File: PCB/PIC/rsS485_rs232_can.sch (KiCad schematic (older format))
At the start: 50 parts, among them J2 TB_1X3, J3 DB9, J4 TB_1X3, U5 MAX3072, U6 ST3232E, U7 MCP2551, U8 PESD1CAN

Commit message: Correcciones al esquematico segun rev01
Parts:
- removed R42, R45: 1K5, ~, symbol R_MINI
- removed U7: MCP2551, ~, symbol MCP2551
- added U7: VP231, footprints:-SOIC8, symbol VP231
- C21, C28: value 10uF / 6V3 -> 10uF/6V3
- D8: footprint ~ -> (none)
- J2, J4: footprint (none) -> footprints:bornier3
- J3: footprint (none) -> footprints:K22X-E9P-NJ
- JP1, JP2, JP3, JP4, JP5, JP6: symbol JUMPER-2 -> Jumper-2
- PS1, PS2: symbol R -> R-RESCUE-ciaa-pic
- U8: footprint (none) -> footprints:SOT23
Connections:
- wire segments 147 -> 144
- no-connect marks 3 -> 5
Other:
- note added: "Quien hizo el 485 y el CAN quería forzar\nla vista del lector. Tamaños de textos estan achicados."
- note added: "SN65HVD230 - 231"
- moved on the sheet: C21, C22, C23, C24, C25, C26, C27, C28, C29, C30, D6, D7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

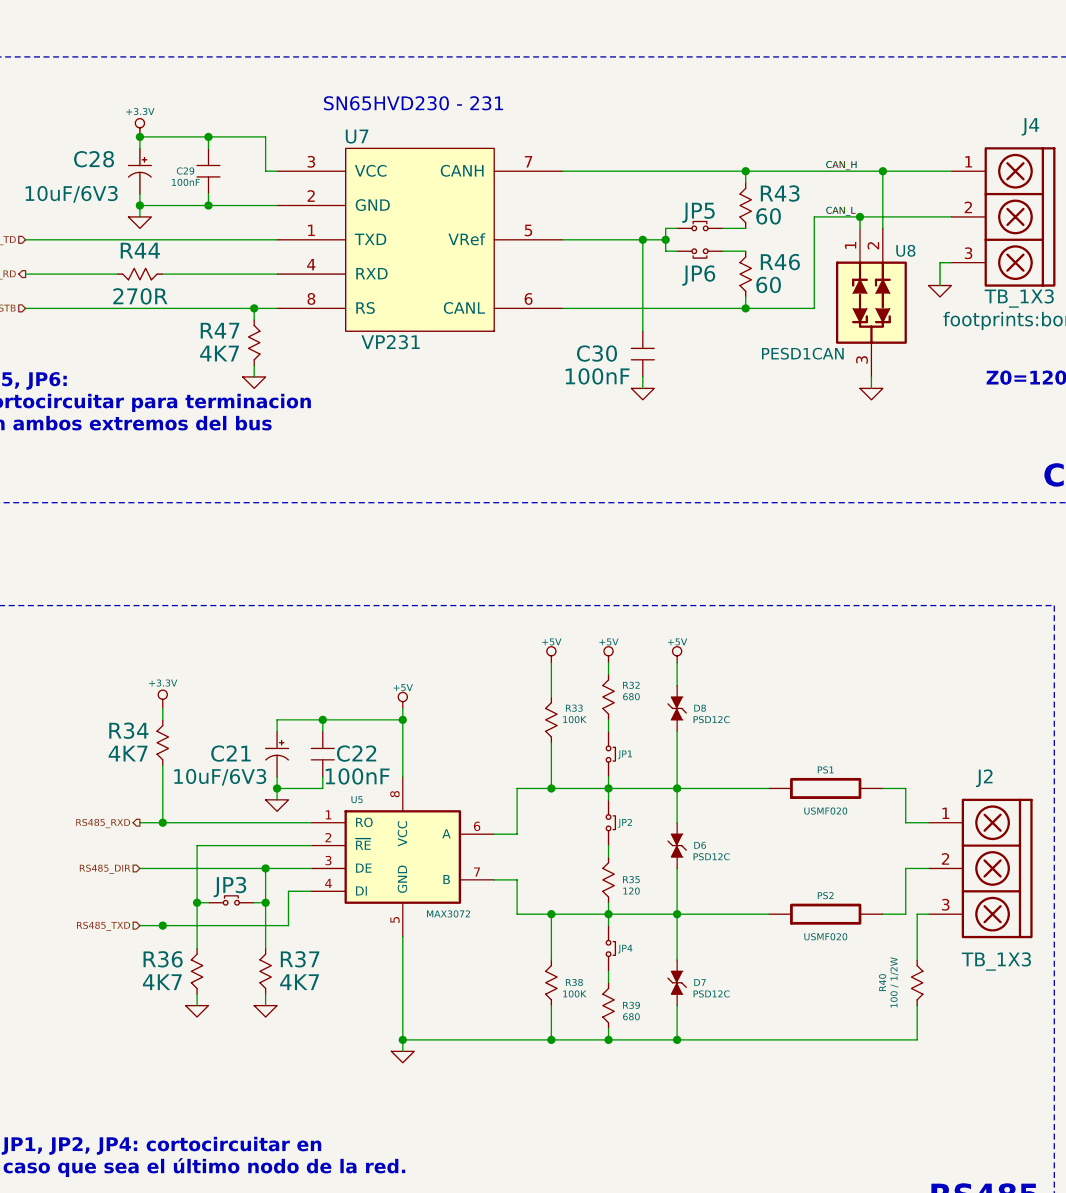
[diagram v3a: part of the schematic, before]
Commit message: elimino conector salida reles
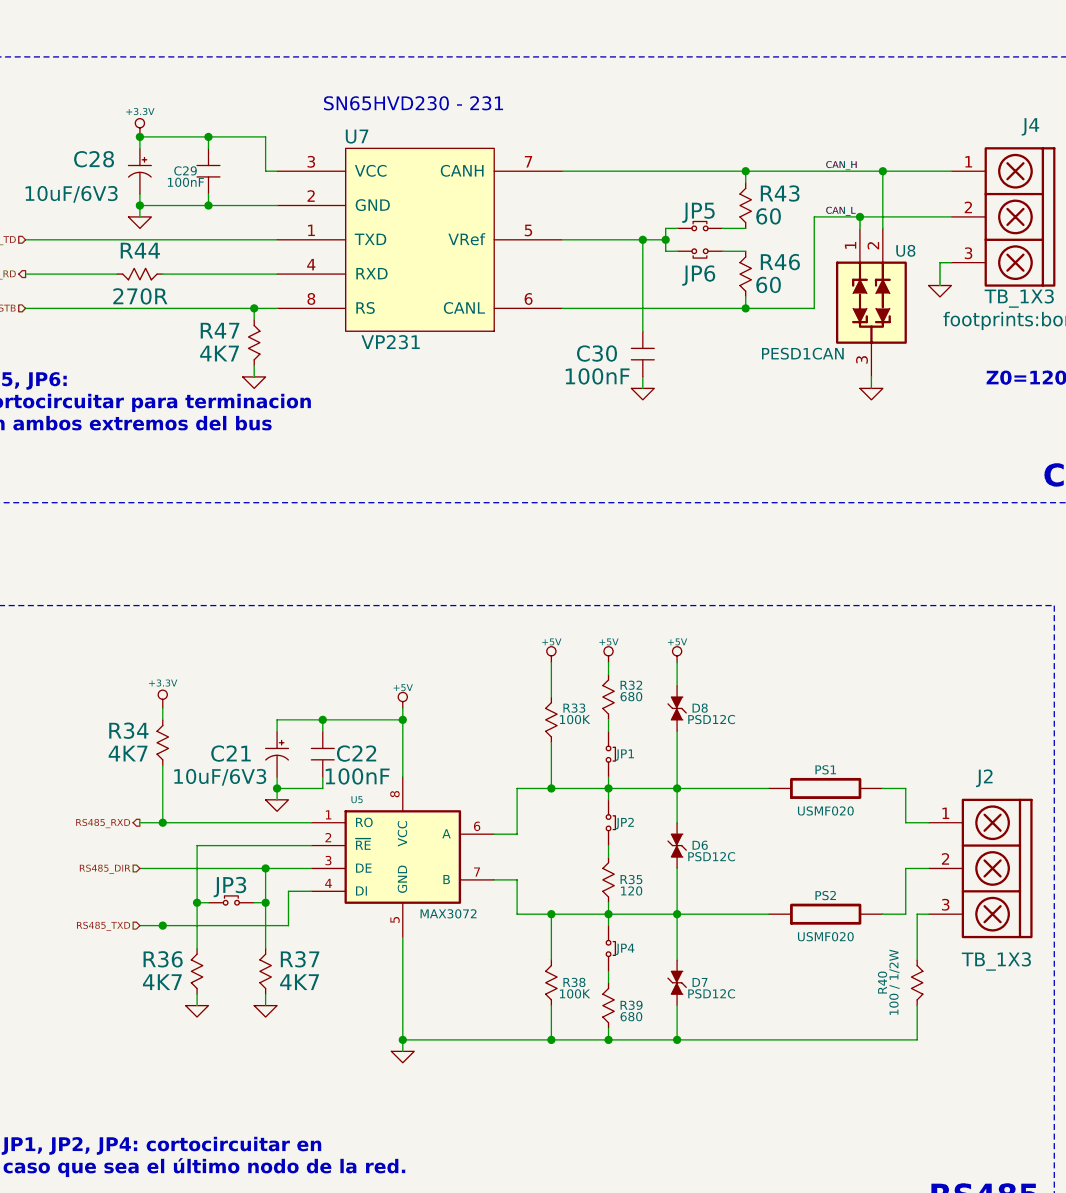
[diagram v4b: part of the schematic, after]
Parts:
- C21, C28, D6, D7, FB12, FB13, FB14, FB17, FB18, FB19, JP1, JP2, JP3, JP4, JP5, JP6, PS1, PS2: footprint ~ -> (none)
- C22, C23, C24, C25, C26, C27, C29, C30: footprint ~ -> Capacitors_SMD:C_0603
- R32, R33, R34, R35, R36, R37, R38, R39, R41, R43, R44, R46, R47: footprint ~ -> Resistors_SMD:R_0603
- R40: footprint ~ -> Resistors_SMD:R_1206

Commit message: rev02 aignacion footprint
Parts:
- U5: footprint SOIC8 -> SMD_Packages:SOIC-8-N
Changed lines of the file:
@@
 F 0 "U5" H 3500 8050 30  0000 C CNN
 F 1 "MAX3072" H 3900 7550 39  0000 C CNN
-F 2 "SOIC8" H 3900 8050 35  0001 C CIN
+F 2 "SMD_Packages:SOIC-8-N" H 3900 8050 35  0001 C CIN
 F 3 "http://www.digikey.com/product-detail/en/maxim-integrated/MAX3072EESA-T/MAX3072EESA-TCT-ND/3647905" H 4350 9000 60  0001 C CNN
 	1    3700 7800

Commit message: rev.02 CIAA-PIC
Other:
- moved on the sheet: C21, C22, C28, C29, C30, D6, D7, D8, J2, J4, JP1, JP2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

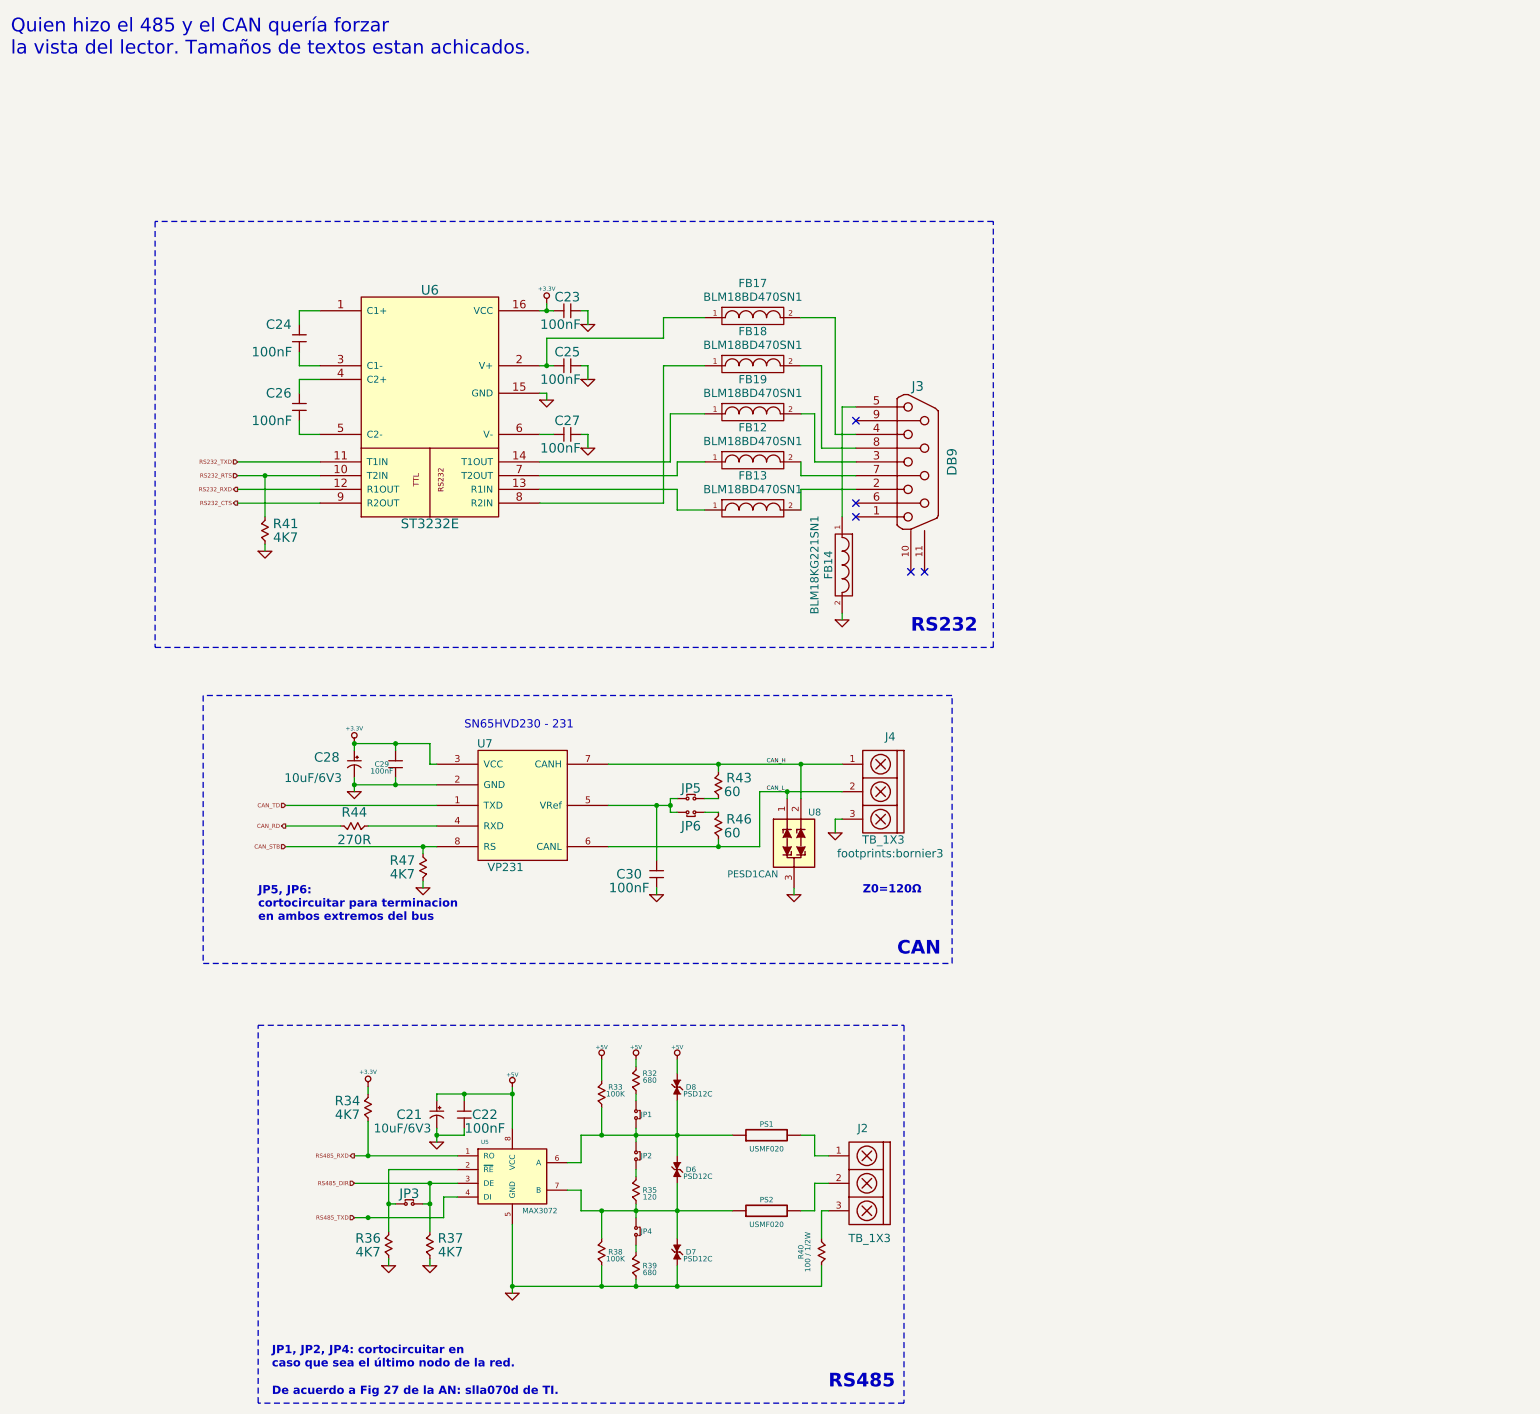
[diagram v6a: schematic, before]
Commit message: rev02 se completa campo num. de frabicante(manf#) CIAA-PIC
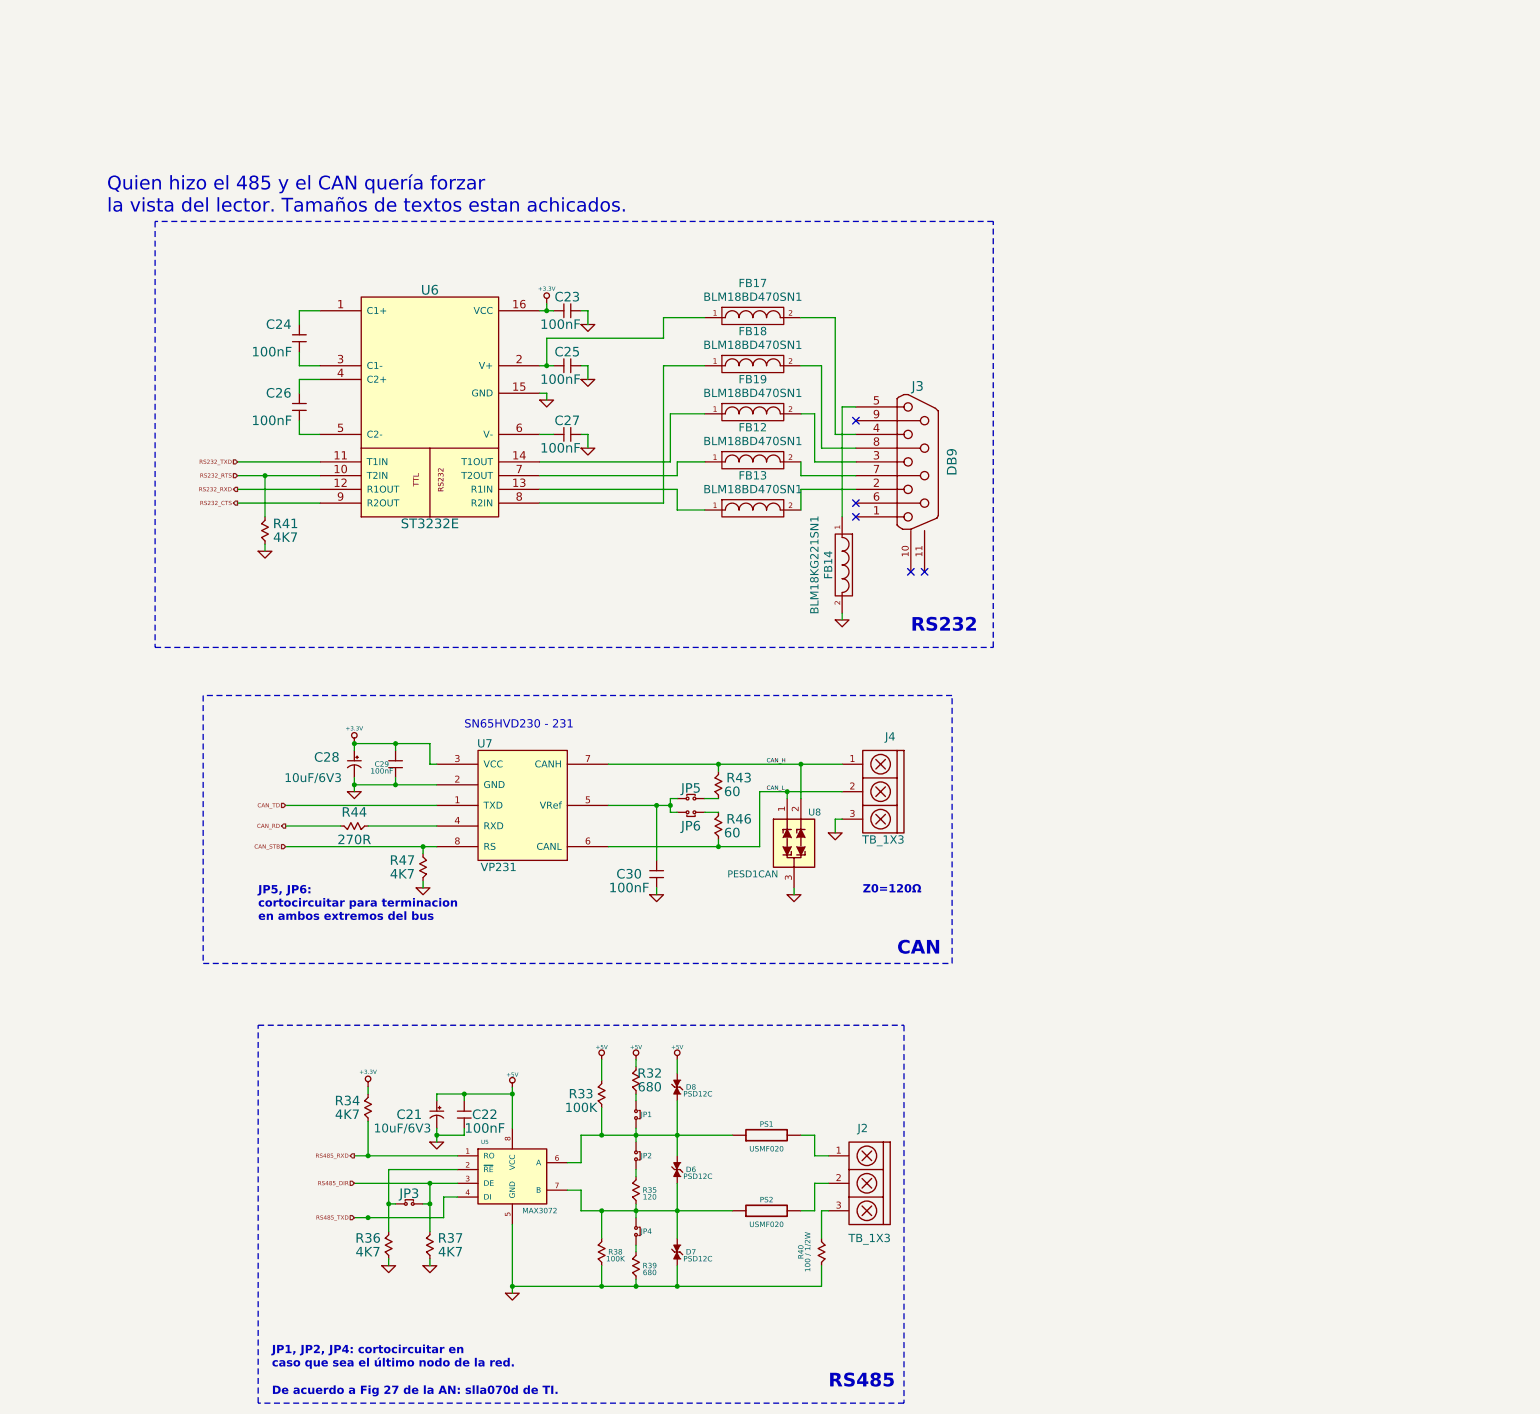
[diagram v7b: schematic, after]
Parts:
- C22, C23, C24, C25, C26, C27, C29, C30: manf# (none) -> C0603C104K5RACTU
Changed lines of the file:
@@
 F 2 "Capacitors_SMD:C_0603" H 3300 7350 60  0001 C CNN
 F 3 "~" H 3300 7350 60  0000 C CNN
+F 4 "C0603C104K5RACTU" V 3300 7350 60  0001 C CNN "manf#"
 	1    3300 7350
 	0    1    1    0
@@
 U 1 1 52C5B34C
 P 4300 7200
-F 0 "R33" V 4350 7100 39  0000 C CNN
-F 1 "100K" V 4300 7100 39  0000 C CNN
+F 0 "R33" V 4300 7350 67  0000 C CNN
+F 1 "100K" V 4200 7350 67  0000 C CNN
 F 2 "Resistors_SMD:R_0603" H 4300 7200 60  0001 C CNN
 F 3 "~" H 4300 7200 60  0000 C CNN
@@
 F 2 "Capacitors_SMD:C_0603" H 2100 1700 60  0001 C CNN
 F 3 "~" H 2100 1700 60  0000 C CNN
+F 4 "C0603C104K5RACTU" V 2100 1700 60  0001 C CNN "manf#"
 	1    2100 1700
 	0    1    1    0
@@
 F 2 "Capacitors_SMD:C_0603" H 2100 2200 60  0001 C CNN
 F 3 "~" H 2100 2200 60  0000 C CNN
+F 4 "C0603C104K5RACTU" V 2100 2200 60  0001 C CNN "manf#"
 	1    2100 2200
 	0    1    1    0
@@
 F 2 "Capacitors_SMD:C_0603" H 4050 1900 60  0001 C CNN
 F 3 "~" H 4050 1900 60  0000 C CNN
+F 4 "C0603C104K5RACTU" H 4050 1900 60  0001 C CNN "manf#"
 	1    4050 1900
 	1    0    0    -1
@@
 F 2 "Capacitors_SMD:C_0603" H 4050 2400 60  0001 C CNN
 F 3 "~" H 4050 2400 60  0000 C CNN
+F 4 "C0603C104K5RACTU" H 4050 2400 60  0001 C CNN "manf#"
 	1    4050 2400
 	1    0    0    -1
@@
 F 2 "Capacitors_SMD:C_0603" H 4050 1500 60  0001 C CNN
 F 3 "~" H 4050 1500 60  0000 C CNN
+F 4 "C0603C104K5RACTU" H 4050 1500 60  0001 C CNN "manf#"
 	1    4050 1500
 	1    0    0    -1
@@
 U 1 1 52C5B362
 P 4550 7100
-F 0 "R32" V 4600 7000 39  0000 C CNN
-F 1 "680" V 4550 7000 39  0000 C CNN
+F 0 "R32" V 4600 7000 67  0000 C CNN
+F 1 "680" V 4500 7000 67  0000 C CNN
 F 2 "Resistors_SMD:R_0603" H 4550 7100 60  0001 C CNN
 F 3 "~" H 4550 7100 60  0000 C CNN
@@
 F 2 "Capacitors_SMD:C_0603" H 2800 4800 60  0001 C CNN
 F 3 "~" H 2800 4800 60  0000 C CNN
+F 4 "C0603C104K5RACTU" V 2800 4800 60  0001 C CNN "manf#"
 	1    2800 4800
 	0    -1   -1   0
@@
 F 0 "J4" H 6400 5200 60  0000 C CNN
 F 1 "TB_1X3" H 6450 4450 60  0000 C CNN
-F 2 "footprints:bornier3" H 6400 4350 60  0000 C CNN
+F 2 "footprints:bornier3" H 6400 4350 60  0001 C CNN
 F 3 "" H 6350 4950 60  0000 C CNN
 	1    6400 4900
@@
 F 2 "Capacitors_SMD:C_0603" H 4700 5600 60  0001 C CNN
 F 3 "~" H 4700 5600 60  0000 C CNN
+F 4 "C0603C104K5RACTU" V 4700 5600 60  0001 C CNN "manf#"
 	1    4700 5600
 	0    1    1    0
@@
 P 3700 5150
 F 0 "U7" H 3450 5650 60  0000 C CNN
-F 1 "VP231" H 3600 4750 60  0000 C CNN
+F 1 "VP231" H 3550 4750 60  0000 C CNN
 F 2 "footprints:-SOIC8" H 3750 4650 60  0001 C CNN
 F 3 "http://www.digikey.com/product-detail/es/texas-instruments/SN65HVD230DR/296-11654-1-ND/404366" H 3900 6100 60  0001 C CNN
@@
 NoConn ~ 6650 3400
 NoConn ~ 6550 3400
-Text Notes 0    -350 0    100  ~ 0
+Text Notes 700  800  0    100  ~ 0
 Quien hizo el 485 y el CAN quería forzar\nla vista del lector. Tamaños de textos estan achicados.
 $EndSCHEMATC

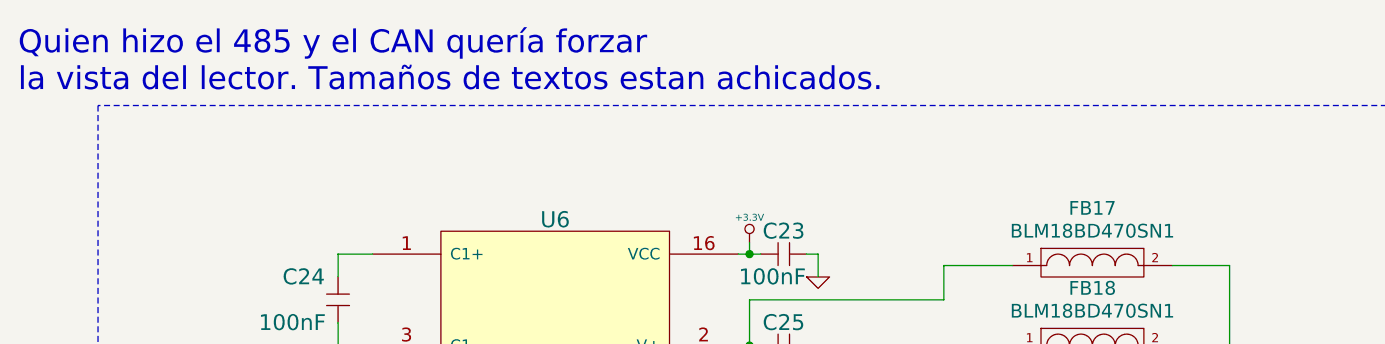
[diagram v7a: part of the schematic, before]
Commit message: se completa campo num. de frabicante(manf#) CIAA-PIC
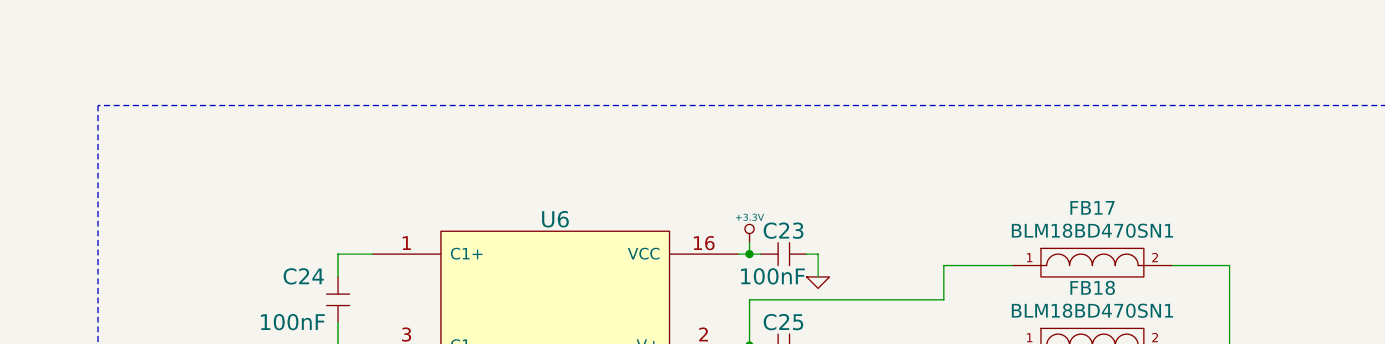
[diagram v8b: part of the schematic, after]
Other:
- note removed: "Quien hizo el 485 y el CAN quería forzar\nla vista del lector. Tamaños de textos estan achicados."
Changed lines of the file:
@@
 NoConn ~ 6650 3400
 NoConn ~ 6550 3400
-Text Notes 700  800  0    100  ~ 0
-Quien hizo el 485 y el CAN quería forzar\nla vista del lector. Tamaños de textos estan achicados.
 $EndSCHEMATC
